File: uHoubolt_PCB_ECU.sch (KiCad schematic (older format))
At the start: 123 parts, among them J1 JST GH, J10 JST GH, J11 Conn_01x02, J12 JST GH, J13 JST GH, J14 206832-0202, J15 206832-0202, J16 206832-0202, J17 206832-0202, J18 206832-0202, J2 JST GH, J3 JST GH, J4 JST GH, J5 JST GH, J6 JST GH, J7 JST GH, J8 Conn_01x04, J9 JST GH, Q1 BSB008NE2LX, Q2 BSB008NE2LX, Q3 BSB008NE2LX, Q4 BSB008NE2LX, Q5 BSB008NE2LX, U1 INAx180x1 (20V/V gain), U10 INAx180x2 (50V/V gain), U11 INAx180x2 (50V/V gain), U12 ICM-20602, U2 INAx180x1 (20V/V gain), U3 INAx180x1 (20V/V gain), U4 INAx180x1 (20V/V gain), U5 INAx180x1 (20V/V gain), U6 SIC431CED-T1-GE3, U7 INAx180x2 (50V/V gain), U8 INAx180x2 (50V/V gain), U9 INAx180x2 (50V/V gain)

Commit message: schematic mostly done
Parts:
- removed D1: RB218NS-60TL, symbol Device:D_Schottky_x2_KCom_KAA
- removed F1, F2, F3: C1H15 (15A fuse), symbol Device:Fuse_Small
- removed J1, J2, J9: JST GH, symbol Connector_Generic_MountingPin:Conn_01x04_MountingPin
- removed J11: Conn_01x02, symbol Connector_Generic:Conn_01x02
- removed J12, J13: JST GH, symbol Connector_Generic:Conn_01x02
- removed J15, J17, J18: 206832-0202, symbol Connector_Generic:Conn_01x02
- removed J8: Conn_01x04, symbol Connector_Generic:Conn_01x04
- removed JP2: SolderJumper_3_Open, symbol Jumper:SolderJumper_3_Open
- removed NT1: Net-Tie_2, symbol Device:Net-Tie_2
- removed Q1, Q2, Q3, Q4, Q5: BSB008NE2LX, Package_DirectFET:DirectFET_MX, symbol Transistor_FET:BSB008NE2LX
- removed R24, R33, R37, R38: 20k, symbol Device:R_Small
- removed R25, R39, R40, R41: 200, symbol Device:R_Small
- removed R26: 1k, symbol Device:R_Small
- removed R30: 6.8k, symbol Device:R_Small
- removed R42, R43, R44: 5m 1W, symbol Device:R_Small
- removed R46, R47: 10k, symbol Device:R_Small
- removed R48, R50, R52: 200k, symbol Device:R_Small
- removed R49, R51, R53: 56k, symbol Device:R_Small
- removed U10, U7, U8, U9: INAx180x2 (50V/V gain), Package_TO_SOT_SMD:SOT-23-6, symbol TXV_LIB:INA180
- removed U2, U3, U4, U5: INAx180x1 (20V/V gain), Package_TO_SOT_SMD:SOT-23-6, symbol TXV_LIB:INA180
- removed U6: SIC431CED-T1-GE3, symbol TXV_LIB:SIC431CED-T1-GE3
- added C1: 100µ, Capacitor_SMD:C_1210_3225Metric, symbol Device:C_Small
- added C21, C26, C27, C31, C32, C33, C34, C35, C38, C41, C42, C43, C46: 100n, Capacitor_SMD:C_0402_1005Metric, symbol Device:C_Small
- added C28, C29, C30: 1u, Capacitor_SMD:C_0603_1608Metric, symbol Device:C_Small
- added C36: 2µ2, Capacitor_SMD:C_0603_1608Metric, symbol Device:C_Small
- added C45: 22µ, Capacitor_SMD:C_0603_1608Metric, symbol Device:C_Small
- added D1: VIN, LED_SMD:LED_0603_1608Metric, symbol Device:LED_Small_ALT
- added D2: PYRO, LED_SMD:LED_0603_1608Metric, symbol Device:LED_Small_ALT
- added D3: TVS Uni, Diode_SMD:D_SOD-123F, symbol Device:D_Schottky_Small_ALT
- added D4: LED 1, LED_SMD:LED_0603_1608Metric, symbol Device:LED_Small_ALT
- added D5: LED 2, LED_SMD:LED_0603_1608Metric, symbol Device:LED_Small_ALT
- added D6: PYRO 1, LED_SMD:LED_0603_1608Metric, symbol Device:LED_Small_ALT
- added D7: OUT 1, LED_SMD:LED_0603_1608Metric, symbol Device:LED_Small_ALT
- added D8: Shottky, Diode_SMD:D_SOD-123F, symbol Device:D_Schottky_Small_ALT
- added J1: Power In, Connector_Molex:Molex_Mega-Fit_76825-0004_2x02_P5.70mm_Horizontal, symbol Connector_Generic:Conn_01x03
- added J2: Debug, Connector_PinHeader_1.27mm:PinHeader_2x04_P1.27mm_Vertical_SMD, symbol Connector_Generic:Conn_02x04_Odd_Even
- added J6: CAN2, Connector_JST:JST_GH_SM04B-GHS-TB_1x04-1MP_P1.25mm_Horizontal, symbol Connector_Generic_MountingPin:Conn_01x04_MountingPin
- added L2: 4µ7, TXV_LIB:SRN4018TA-4R7M, symbol Device:L_Small
- added LS1: Speaker, TXV_LIB:Piezo_Buzzer, symbol Device:Speaker_Crystal
- added Q1: SISA88DN or similar, TXV_LIB:PowerPAK_1212-8, symbol Device:Q_NMOS_GDS
- added R12: 6.8k, Resistor_SMD:R_0603_1608Metric, symbol Device:R_Small
- added R2: 200k, Resistor_SMD:R_0603_1608Metric, symbol Device:R_Small
- added R3, R6: LED, Resistor_SMD:R_0603_1608Metric, symbol Device:R_Small
- added U1: SiC431CED-T1-GE3, TXV_LIB:SiC431AEDT1GE3, symbol TXV_LIB:SiC431CED-T1-GE3
- added U2: TS30041-M050QFNR, Package_DFN_QFN:QFN-16-1EP_3x3mm_P0.5mm_EP1.75x1.75mm_ThermalVias, symbol TXV_LIB:TS30041
- added U3: MCP1700-3302E, Package_TO_SOT_SMD:SOT-23, symbol Regulator_Linear:MCP1700-3302E_SOT23
- added U4, U5: MCP2562FDT-H_SN, Package_DFN_QFN:DFN-8-1EP_3x3mm_P0.65mm_EP1.55x2.4mm, symbol TXV_LIB:MCP2562FDT-H_SN
- added U6: STM32G491MET6-LQFP80, Package_QFP:LQFP-80_14x14mm_P0.65mm, symbol TXV_LIB:STM32G491MET6-LQFP80
- added U8: W25Q256JV, TXV_LIB:WSON-8-8x6mm, symbol TXV_LIB:W25Q256JV
- added U9: TPS1HC100, Package_SO:HTSSOP-14-1EP_4.4x5mm_P0.65mm_EP3.4x5mm_Mask3x3.1mm, symbol TXV_LIB:TPS1HC100
- added X1: TXC-7C, Oscillator:Oscillator_SMD_TXC_7C-4Pin_5.0x3.2mm, symbol Oscillator:TXC-7C
- C10: value C_Small -> 10µ; footprint (none) -> Capacitor_SMD:C_0603_1608Metric
- C11, C6: value 33u -> 100µ; footprint (none) -> Capacitor_SMD:C_1210_3225Metric
- C12, C17: value 100u -> 100n; footprint (none) -> Capacitor_SMD:C_0402_1005Metric
- C13, C15: value 100u -> 100µ; footprint (none) -> Capacitor_SMD:C_1210_3225Metric
- C14: value 4.7u -> 100µ; footprint (none) -> Capacitor_SMD:C_1210_3225Metric
- C16: value 33u -> 2µ2; footprint (none) -> Capacitor_SMD:C_0603_1608Metric
- C18: value 1u -> 22µ; footprint (none) -> Capacitor_SMD:C_0603_1608Metric
- C19: value 100n -> 22µ; footprint (none) -> Capacitor_SMD:C_0603_1608Metric
- C2, C5: value 100n -> 100µ; footprint (none) -> Capacitor_SMD:C_1210_3225Metric
- C20: value 100n -> 2µ2; footprint (none) -> Capacitor_SMD:C_0603_1608Metric
- C22: value 2.2u -> 100n; footprint (none) -> Capacitor_SMD:C_0402_1005Metric
- C23, C24, C8: footprint (none) -> Capacitor_SMD:C_0402_1005Metric
- C25: value 100n -> 10n; footprint (none) -> Capacitor_SMD:C_0402_1005Metric
- C3: value 100n -> 4µ7; footprint (none) -> Capacitor_SMD:C_0603_1608Metric
- C37: renamed from C21; footprint (none) -> Capacitor_SMD:C_0402_1005Metric
- C39: renamed from C26; footprint (none) -> Capacitor_SMD:C_0402_1005Metric
- C4: value 100n -> 1µ; footprint (none) -> Capacitor_SMD:C_0603_1608Metric
- C40: renamed from C27; footprint (none) -> Capacitor_SMD:C_0402_1005Metric
- C44: renamed from C1; footprint (none) -> Capacitor_SMD:C_0402_1005Metric
- C7, C9: value 33u -> 100n; footprint (none) -> Capacitor_SMD:C_0402_1005Metric
- J10: renamed from J6; value JST GH -> Servo 1; footprint (none) -> Connector_Molex:Molex_Nano-Fit_105313-xx04_1x04_P2.50mm_Horizontal; symbol Connector_Generic_MountingPin:Conn_01x04_MountingPin -> Connector_Generic:Conn_01x04
- J11: renamed from J16; value 206832-0202 -> PYRO 1; footprint (none) -> Connector_Molex:Molex_SL_171971-0002_1x02_P2.54mm_Vertical; Male Mate 206461-0200 -> (none); Mate Datasheet https://www.mouser.at/datasheet/2/276/2/2064610200_CRIMP_HO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 -> (none)
- J3, J5: value JST GH -> CAN1; footprint (none) -> Connector_JST:JST_GH_SM04B-GHS-TB_1x04-1MP_P1.25mm_Horizontal
- J4: value JST GH -> CAN2; footprint (none) -> Connector_JST:JST_GH_SM04B-GHS-TB_1x04-1MP_P1.25mm_Horizontal
- J7: value JST GH -> Pressure 1; footprint (none) -> Connector_JST:JST_GH_SM04B-GHS-TB_1x04-1MP_P1.25mm_Horizontal
- J8: renamed from J10; value JST GH -> TEMP 1; footprint (none) -> Connector_JST:JST_GH_BM02B-GHS-TBT_1x02-1MP_P1.25mm_Vertical
- J9: renamed from J14; value 206832-0202 -> OUT 1; footprint (none) -> Connector_Molex:Molex_Nano-Fit_105313-xx02_1x02_P2.50mm_Horizontal; Male Mate 206461-0200 -> (none); Mate Datasheet https://www.mouser.at/datasheet/2/276/2/2064610200_CRIMP_HO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 -> (none)
- JP1: value SolderJumper_3_Open -> V_SEL; footprint (none) -> Jumper:SolderJumper-3_P1.3mm_Open_RoundedPad1.0x1.5mm
- L1: value 5.3u -> 820nH; footprint (none) -> Inductor_SMD:L_Vishay_IHLP-6767
- R1: value 20k -> 100k; footprint (none) -> Resistor_SMD:R_0603_1608Metric
- R10: value 33k -> 115k; footprint (none) -> Resistor_SMD:R_0603_1608Metric; Mouser (none) -> https://www.mouser.at/ProductDetail/Vishay-Dale/CRCW0201115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
- R11, R16, R36, R8: value 20k -> 10k; footprint (none) -> Resistor_SMD:R_0603_1608Metric
- R13: footprint (none) -> Resistor_SMD:R_0603_1608Metric
- R14: value 6.8k -> 10k; footprint (none) -> Resistor_SMD:R_0603_1608Metric
- R15: value R_Small -> 2k; footprint (none) -> Resistor_SMD:R_0603_1608Metric
- R17: value 47k -> 120; footprint (none) -> Resistor_SMD:R_0603_1608Metric
- R18: value 33k -> 120; footprint (none) -> Resistor_SMD:R_0603_1608Metric
- R19: value 1k -> LED; footprint (none) -> Resistor_SMD:R_0603_1608Metric
- R20: value 51k -> LED; footprint (none) -> Resistor_SMD:R_0603_1608Metric
- R21: value 499k -> LED; footprint (none) -> Resistor_SMD:R_0603_1608Metric
- R22: value 115k -> 22k; footprint (none) -> Resistor_SMD:R_0603_1608Metric; Mouser https://www.mouser.at/ProductDetail/Vishay-Dale/CRCW0201115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 -> (none)
- R23: value 10k -> LED; footprint (none) -> Resistor_SMD:R_0603_1608Metric
- R24: renamed from R6; value 47k -> 10k; footprint (none) -> Resistor_SMD:R_0603_1608Metric
- R25: renamed from R2; value 4.7k/0 -> 4k7/0; footprint (none) -> Resistor_SMD:R_0603_1608Metric
- R26: renamed from R3; value 6.8k/160 -> 6k8/160; footprint (none) -> Resistor_SMD:R_0603_1608Metric
- R27: footprint (none) -> Resistor_SMD:R_0603_1608Metric; Mouser https://www.mouser.at/ProductDetail/Vishay-Dale/CRCW0201115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 -> (none)
- R28, R35: value 5m 1W -> 1k; footprint (none) -> Resistor_SMD:R_0603_1608Metric; Type ULR1S-R005FT2 -> (none)
- R29: value 4.7k -> 10m 1W; footprint (none) -> Resistor_SMD:R_1206_3216Metric; Type (none) -> ULR1S-R005FT2
- R30: renamed from R12; footprint (none) -> Resistor_SMD:R_0603_1608Metric
- R31: value 6.8k -> 10m 1W; footprint (none) -> Resistor_SMD:R_1206_3216Metric; Type (none) -> ULR1S-R005FT2
- R32: value 4.7k -> 1k; footprint (none) -> Resistor_SMD:R_0603_1608Metric
- R33: renamed from R45; footprint (none) -> Resistor_SMD:R_0603_1608Metric
- R34: value 200 -> 10k; footprint (none) -> Resistor_SMD:R_0603_1608Metric
- R4: value 4.7k/0 -> 10k; footprint (none) -> Resistor_SMD:R_0603_1608Metric
- R5: value 6.8k/160 -> 2k; footprint (none) -> Resistor_SMD:R_0603_1608Metric
- R7: value 33k -> 3R3; footprint (none) -> Resistor_SMD:R_0603_1608Metric
- R9: value 47k -> 2k; footprint (none) -> Resistor_SMD:R_0603_1608Metric
- U10: renamed from U1; value INAx180x1 (20V/V gain) -> INA180A1
- U11: value INAx180x2 (50V/V gain) -> INA180A1
- renumbered U12 to U7
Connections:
- net labels added: +7.4V, 12V_SENSE, 7V4_EN, 7V4_PGOOD, 7V4_SENSE, CAN1_H, CAN1_L, CAN1_RX, CAN1_TX, CAN2_H, CAN2_L, CAN2_RX, CAN2_TX, CLK, IMU_INT, LED_1, LED_2, NRST, OUT_1_CTRL, OUT_1_CURR, PRESS_1, PYRO_1_CONT, PYRO_1_CTRL, PYRO_1_CURR, PYRO_SENSE, Pyro, QSPI1_BK1_IO0, QSPI1_BK1_IO1, QSPI1_BK1_IO2, QSPI1_BK1_IO3, QSPI1_BK1_NCS, QSPI1_CLK, SERVO_1_CURR, SERVO_1_FDBK, SERVO_1_PWM, SPI_SCK, SWCLK, SWDIO, Speaker_N, Speaker_P, TEMP_1, UART4_RX, UART4_TX
- net labels removed: +7.5V, 7V5_SENSE, A_GND, GNDA, IGNITECONTINUITY1, IGNITECONTINUITY2, IGNITECONTINUITY3, IGNITECONTROL1, IGNITECONTROL2, IGNITECONTROL3, IGNITESENSE1, IGNITESENSE2, IGNITESENSE3, IMU_INTERRUPT, PRESSURESENSE1, PRESSURESENSE2, PRESSURESENSE3, SERVO1_FDBK, SERVO1_PWM, SERVO2_FDBK, SERVO2_PWM, SERVO3_FDBK, SERVO3_PWM, SOLCONTROL1, SOLCONTROL2, SOLSENSE1, SOLSENSE2, SPI_CLK, TEMP1, TEMP2, TEMP3, TESTPRESSURESENSE1, TESTPRESSURESENSE2, VOLTREG_EN, VOLTREG_P_GOOD, Vdrive
- wire segments 601 -> 582
- no-connect marks 6 -> 8
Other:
- note added: "(Gain 20)"
- note added: "1k*Iout/1040"
- note added: "2x"
- note added: "3x"
- note added: "5x"
- note added: "Analog max. 26, 2 zu wenig"
- note added: "CAN"
- note added: "Digital max. 20x"
- note added: "High Current Outputs"
- note added: "IMU"
- note added: "MCU + QSPI FLASH + LEDs + Speaker"
- note added: "NTC Inputs"
- note added: "Pressure Sensor Inputs"
- note added: "Pyro outputs"
- note added: "R_ILIM = 22k\n--> 2A Current Limit"
- note added: "Servo outputs"
- note added: "TODO: Molex 2002411223"
- note added: "TODO: Molex SL Horizontal"
- note added: "To PGA in STM"
- note added: "Voltage Regulators"
- note removed: "(NTC): RC low-pass can use other component values \nif 33u SMD is hard to find"
- note removed: "- if using INA180 -> place on high-side of circuit, above MOSFET.\n in case of other OP-AMP: choose one with rail-to-rail amplification!\n- if necessary, replace MOS with another model"
- note removed: "12V"
- note removed: "5V SENSING"
- note removed: "7.4V SENSING"
- note removed: "7.4V Voltage Reg"
- note removed: "BATT3V6"
- note removed: "BATT7V2"
- note removed: "BATT_GND"
- note removed: "BATT_VCC"
- note removed: "GND/A_GND NET TIE"
- note removed: "IMU - SPI interface"
- note removed: "NTC: TG250J34GBNR, 5k Ohm\nhttps://www.mouser.at/datasheet/2/18/Amphenol_2017.06.15_Datasheet_CIG_thermistor-1730609.pdf"
- note removed: "NTCs"
- note removed: "PMU Voltage Inputs"
- note removed: "PRESSURE GROUND TESTING"
- note removed: "PRESSURE SENSING"
- note removed: "PYRO/IGNITION"
- note removed: "SERVOs"
- note removed: "SOLENOIDS"
- note removed: "connects to PMU connector\nin IGNITION circuit"
- note removed: "connects to uHoubold_PCB_PMU\n"J_BALANCE1" connector"
- note removed: "keine Elektrolyt-C!\nMan kriegt in Keramik keine 100u"
- moved on the sheet: C37, C39, C40, C44, J11, J8, J9, JP1, R24, R25, R26, R30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

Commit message: schematic even more done
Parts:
- removed C24: 100n, Capacitor_SMD:C_0402_1005Metric, symbol Device:C_Small
- added JP2: VDD, Jumper:SolderJumper-2_P1.3mm_Bridged_RoundedPad1.0x1.5mm, symbol Device:Jumper_NC_Small
- added JP3: VDRV, Jumper:SolderJumper-2_P1.3mm_Bridged_RoundedPad1.0x1.5mm, symbol Device:Jumper_NC_Small
- C10: value 10µ -> 100µ; footprint Capacitor_SMD:C_0603_1608Metric -> Capacitor_SMD:C_1210_3225Metric
- C25: value 10n -> 100n
- C28, C29: value 1u -> 2µ2
- C3: value 4µ7 -> 22µ
- C30: value 1u -> 100n; footprint Capacitor_SMD:C_0603_1608Metric -> Capacitor_SMD:C_0402_1005Metric
- C4: value 1µ -> 2µ2
- J1: footprint Connector_Molex:Molex_Mega-Fit_76825-0004_2x02_P5.70mm_Horizontal -> TXV_LIB:Molex_MegaFit_1x03
- J11: footprint Connector_Molex:Molex_SL_171971-0002_1x02_P2.54mm_Vertical -> TXV_LIB:Molex_SL_1x2
- J8: symbol Connector_Generic:Conn_01x02 -> Connector_Generic_MountingPin:Conn_01x02_MountingPin
- R10: value 115k -> 100k
- R11, R14, R16, R24, R27, R34, R4, R8: value 10k -> 9k1
- R12: value 6.8k -> 22k
- R13: value 4.7k -> 9k1
- R15: value 2k -> 9k1
- R19, R20, R21, R23: value LED -> 120
- R28: value 1k -> 120
- R3, R6: value LED -> 1k
- R33, R36: value 10k -> 22k
- R5, R9: value 2k -> 1k
- U1: value SiC431CED-T1-GE3 -> SiC431C
- U10, U11: value INA180A1 -> INA180B1; footprint Package_TO_SOT_SMD:SOT-23-6 -> Package_TO_SOT_SMD:SOT-23-5; symbol TXV_LIB:INA180 -> TXV_LIB:INA180B
- U5: value MCP2562FDT-H_SN -> MCP2562FDT; symbol TXV_LIB:MCP2562FDT-H_SN -> TXV_LIB:MCP2562FDT
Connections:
- wire segments 582 -> 615
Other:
- note added: "2x PGA Input"
- note added: "Analog max. 26, aktuell 25"
- note added: "Analog?"
- note added: "For SiC431A/B, open\nVDD and VDRV jumpers"
- note added: "TODO: Snubber/tantal In+Out"
- note added: "resistors chosen for 7.2V\nto consolidate BOM"
- note removed: "Analog max. 26, 2 zu wenig"
- note removed: "TODO: Molex 2002411223"
- note removed: "TODO: Molex SL Horizontal"
- moved on the sheet: C25, C28, C29

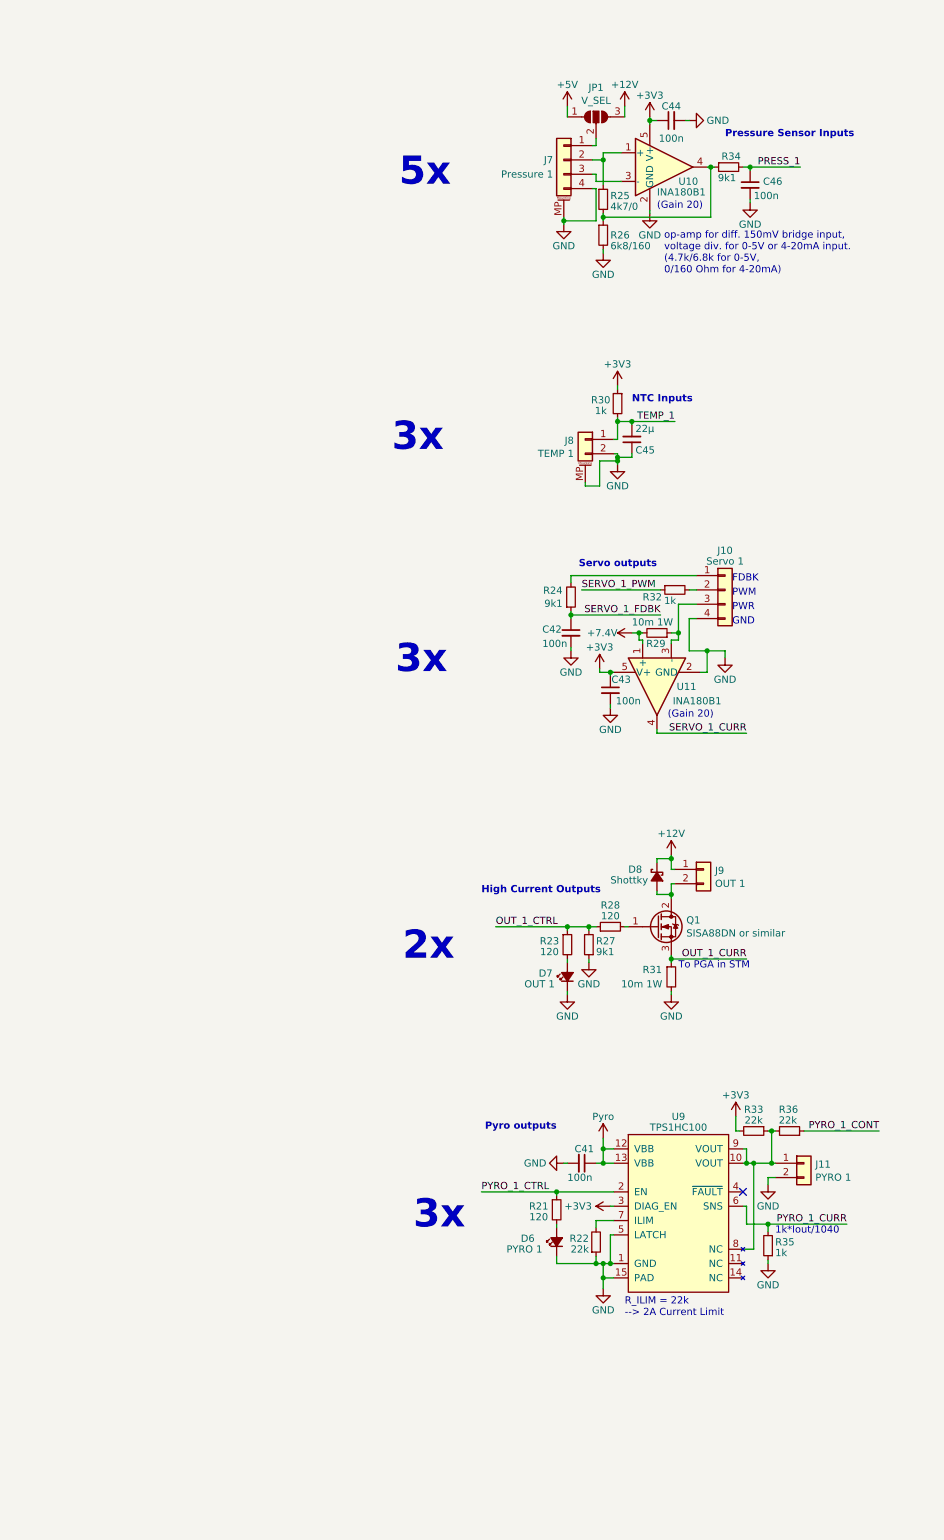
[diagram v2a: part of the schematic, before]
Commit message: moved I/O to subsheets, started layout
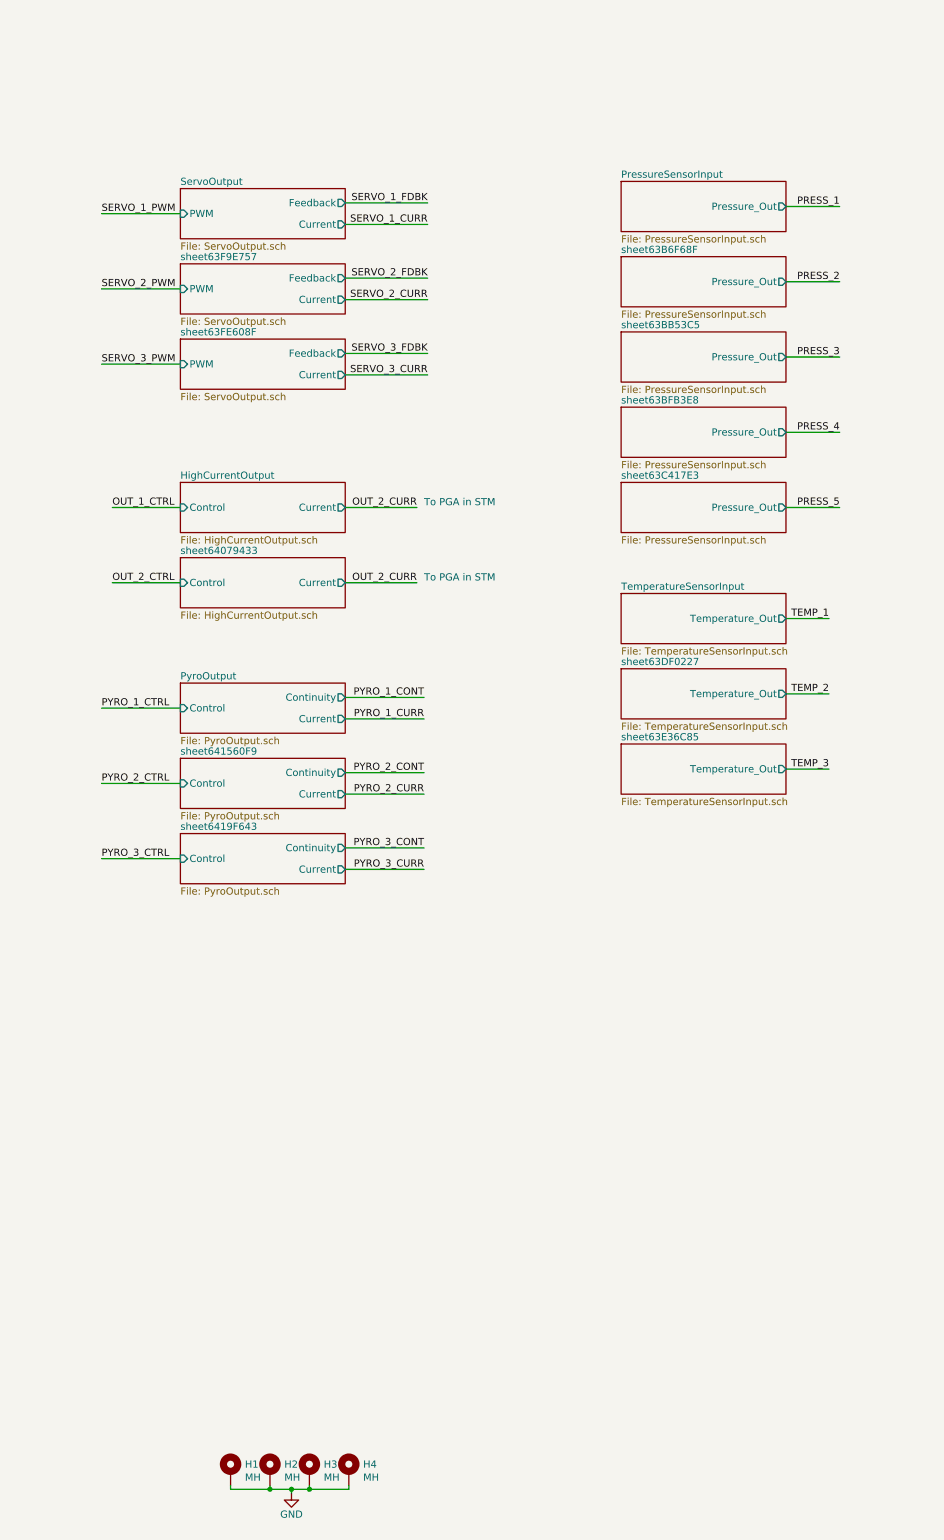
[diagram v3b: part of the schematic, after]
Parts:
- removed C41, C42, C43, C44, C46: 100n, Capacitor_SMD:C_0402_1005Metric, symbol Device:C_Small
- removed C45: 22µ, Capacitor_SMD:C_0603_1608Metric, symbol Device:C_Small
- removed D6: PYRO 1, LED_SMD:LED_0603_1608Metric, symbol Device:LED_Small_ALT
- removed D7: OUT 1, LED_SMD:LED_0603_1608Metric, symbol Device:LED_Small_ALT
- removed D8: Shottky, Diode_SMD:D_SOD-123F, symbol Device:D_Schottky_Small_ALT
- removed J10: Servo 1, Connector_Molex:Molex_Nano-Fit_105313-xx04_1x04_P2.50mm_Horizontal, symbol Connector_Generic:Conn_01x04
- removed J11: PYRO 1, TXV_LIB:Molex_SL_1x2, symbol Connector_Generic:Conn_01x02
- removed J7: Pressure 1, Connector_JST:JST_GH_SM04B-GHS-TB_1x04-1MP_P1.25mm_Horizontal, symbol Connector_Generic_MountingPin:Conn_01x04_MountingPin
- removed J8: TEMP 1, Connector_JST:JST_GH_BM02B-GHS-TBT_1x02-1MP_P1.25mm_Vertical, symbol Connector_Generic_MountingPin:Conn_01x02_MountingPin
- removed J9: OUT 1, Connector_Molex:Molex_Nano-Fit_105313-xx02_1x02_P2.50mm_Horizontal, symbol Connector_Generic:Conn_01x02
- removed JP1: V_SEL, Jumper:SolderJumper-3_P1.3mm_Open_RoundedPad1.0x1.5mm, symbol Jumper:SolderJumper_3_Open
- removed Q1: SISA88DN or similar, TXV_LIB:PowerPAK_1212-8, symbol Device:Q_NMOS_GDS
- removed R21, R23, R28: 120, Resistor_SMD:R_0603_1608Metric, symbol Device:R_Small
- removed R22, R33, R36: 22k, Resistor_SMD:R_0603_1608Metric, symbol Device:R_Small
- removed R24, R27, R34: 9k1, Resistor_SMD:R_0603_1608Metric, symbol Device:R_Small
- removed R25: 4k7/0, Resistor_SMD:R_0603_1608Metric, symbol Device:R_Small
- removed R26: 6k8/160, Resistor_SMD:R_0603_1608Metric, symbol Device:R_Small
- removed R29, R31: 10m 1W, Resistor_SMD:R_1206_3216Metric, symbol Device:R_Small
- removed R30, R32, R35: 1k, Resistor_SMD:R_0603_1608Metric, symbol Device:R_Small
- removed U10, U11: INA180B1, Package_TO_SOT_SMD:SOT-23-5, symbol TXV_LIB:INA180B
- removed U9: TPS1HC100, Package_SO:HTSSOP-14-1EP_4.4x5mm_P0.65mm_EP3.4x5mm_Mask3x3.1mm, symbol TXV_LIB:TPS1HC100
- added H1, H2, H3, H4: MH, MountingHole:MountingHole_3.2mm_M3_Pad_Via, symbol Mechanical:MountingHole_Pad
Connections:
- net labels added: OUT_2_CTRL, OUT_2_CURR, PRESS_2, PRESS_3, PRESS_4, PRESS_5, PYRO_2_CONT, PYRO_2_CTRL, PYRO_2_CURR, PYRO_3_CONT, PYRO_3_CTRL, PYRO_3_CURR, SERVO_2_CURR, SERVO_2_FDBK, SERVO_2_PWM, SERVO_3_CURR, SERVO_3_FDBK, SERVO_3_PWM, TEMP_2, TEMP_3
- wire segments 615 -> 503
- no-connect marks 8 -> 7
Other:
- note removed: "(Gain 20)"
- note removed: "1k*Iout/1040"
- note removed: "2x"
- note removed: "3x"
- note removed: "5x"
- note removed: "FDBK"
- note removed: "GND"
- note removed: "High Current Outputs"
- note removed: "NTC Inputs"
- note removed: "PWM"
- note removed: "PWR\n"
- note removed: "Pressure Sensor Inputs"
- note removed: "Pyro outputs"
- note removed: "R_ILIM = 22k\n--> 2A Current Limit"
- note removed: "Servo outputs"
- note removed: "op-amp for diff. 150mV bridge input,\nvoltage div. for 0-5V or 4-20mA input.\n(4.7k/6.8k for 0-5V,\n0/160 Ohm for 4-20mA)"

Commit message: preliminary placement done
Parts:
- D1: Label (none) -> 12V
- D2: Label (none) -> Pyro
- D4: Label (none) -> 1
- D5: Label (none) -> 2
- J3, J4, J5, J6: footprint Connector_JST:JST_GH_SM04B-GHS-TB_1x04-1MP_P1.25mm_Horizontal -> Connector_JST:JST_GH_BM04B-GHS-TBT_1x04-1MP_P1.25mm_Vertical
- U4: symbol TXV_LIB:MCP2562FDT-H_SN -> TXV_LIB:MCP2562FDT
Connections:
- wire segments 503 -> 506
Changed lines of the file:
@@
 F 2 "LED_SMD:LED_0603_1608Metric" V 2350 1275 50  0001 C CNN
 F 3 "~" V 2350 1275 50  0001 C CNN
+F 4 "Pyro" V 2350 1275 50  0001 C CNN "Label"
 	1    2350 1275
 	0    -1   -1   0
@@
 F 2 "LED_SMD:LED_0603_1608Metric" V 1500 1275 50  0001 C CNN
 F 3 "~" V 1500 1275 50  0001 C CNN
+F 4 "12V" V 1500 1275 50  0001 C CNN "Label"
 	1    1500 1275
 	0    -1   -1   0
@@
 F 2 "LED_SMD:LED_0603_1608Metric" V 1525 4325 50  0001 C CNN
 F 3 "~" V 1525 4325 50  0001 C CNN
+F 4 "2" H 1525 4325 50  0001 C CNN "Label"
 	1    1525 4325
 	-1   0    0    -1
@@
 F 2 "LED_SMD:LED_0603_1608Metric" V 1525 4125 50  0001 C CNN
 F 3 "~" V 1525 4125 50  0001 C CNN
+F 4 "1" H 1525 4125 50  0001 C CNN "Label"
 	1    1525 4125
 	-1   0    0    -1
@@
 F 0 "J4" H 6650 10325 50  0000 L CNN
 F 1 "CAN2" H 6650 10225 50  0000 L CNN
-F 2 "Connector_JST:JST_GH_SM04B-GHS-TB_1x04-1MP_P1.25mm_Horizontal" H 6575 10325 50  0001 C CNN
+F 2 "Connector_JST:JST_GH_BM04B-GHS-TBT_1x04-1MP_P1.25mm_Vertical" H 6575 10325 50  0001 C CNN
 F 3 "~" H 6575 10325 50  0001 C CNN
 	1    6575 10325
@@
 F 0 "J6" H 7350 10325 50  0000 L CNN
 F 1 "CAN2" H 7350 10225 50  0000 L CNN
-F 2 "Connector_JST:JST_GH_SM04B-GHS-TB_1x04-1MP_P1.25mm_Horizontal" H 7275 10325 50  0001 C CNN
+F 2 "Connector_JST:JST_GH_BM04B-GHS-TBT_1x04-1MP_P1.25mm_Vertical" H 7275 10325 50  0001 C CNN
 F 3 "~" H 7275 10325 50  0001 C CNN
 	1    7275 10325
@@
 F 0 "J3" H 6650 8900 50  0000 L CNN
 F 1 "CAN1" H 6650 8800 50  0000 L CNN
-F 2 "Connector_JST:JST_GH_SM04B-GHS-TB_1x04-1MP_P1.25mm_Horizontal" H 6575 8900 50  0001 C CNN
+F 2 "Connector_JST:JST_GH_BM04B-GHS-TBT_1x04-1MP_P1.25mm_Vertical" H 6575 8900 50  0001 C CNN
 F 3 "~" H 6575 8900 50  0001 C CNN
 	1    6575 8900
@@
 $EndComp
 $Comp
-L TXV_LIB:MCP2562FDT-H_SN U?
+L TXV_LIB:MCP2562FDT U?
 U 1 1 6322A030
 P 5075 8975
@@
 F 0 "J5" H 7350 8900 50  0000 L CNN
 F 1 "CAN1" H 7350 8800 50  0000 L CNN
-F 2 "Connector_JST:JST_GH_SM04B-GHS-TB_1x04-1MP_P1.25mm_Horizontal" H 7275 8900 50  0001 C CNN
+F 2 "Connector_JST:JST_GH_BM04B-GHS-TBT_1x04-1MP_P1.25mm_Vertical" H 7275 8900 50  0001 C CNN
 F 3 "~" H 7275 8900 50  0001 C CNN
 	1    7275 8900
@@
 	4925 8475 4925 8550
 Wire Wire Line
-	5075 9375 5075 9425
+	5075 9375 5075 9400
 $Comp
 L power:+3V3 #PWR?
@@
 Wire Wire Line
 	12025 6525 11475 6525
+Wire Wire Line
+	5175 9375 5175 9400
+Wire Wire Line
+	5175 9400 5075 9400
+Connection ~ 5075 9400
+Wire Wire Line
+	5075 9400 5075 9425
 $EndSCHEMATC

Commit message: changed form factor to better fit into uHb engine section
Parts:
- J1: footprint TXV_LIB:Molex_MegaFit_1x03 -> TXV_LIB:Molex_MegaFit_1x03_Vertical
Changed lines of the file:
@@
 F 0 "J1" H 775 1425 50  0000 C CNN
 F 1 "Power In" H 775 1350 50  0000 C CNN
-F 2 "TXV_LIB:Molex_MegaFit_1x03" H 775 1150 50  0001 C CNN
+F 2 "TXV_LIB:Molex_MegaFit_1x03_Vertical" H 775 1150 50  0001 C CNN
 F 3 "~" H 775 1150 50  0001 C CNN
 	1    775  1150
